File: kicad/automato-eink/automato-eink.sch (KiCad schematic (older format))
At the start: 20 parts

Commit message: finish schematic capture
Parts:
- added J?: Conn_01x08_Male, Connector_PinHeader_2.54mm:PinHeader_1x08_P2.54mm_Vertical, symbol Connector:Conn_01x08_Male
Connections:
- net labels added: BS, BUSY, CS, DC, GDR, HLT_CTL, PREVGH, PREVGL, RESE, RST, SCLK, SDI, TSCL, TSDA
- wire segments 52 -> 74
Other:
- moved on the sheet: C?, D?, J?, L?, Q?, R?

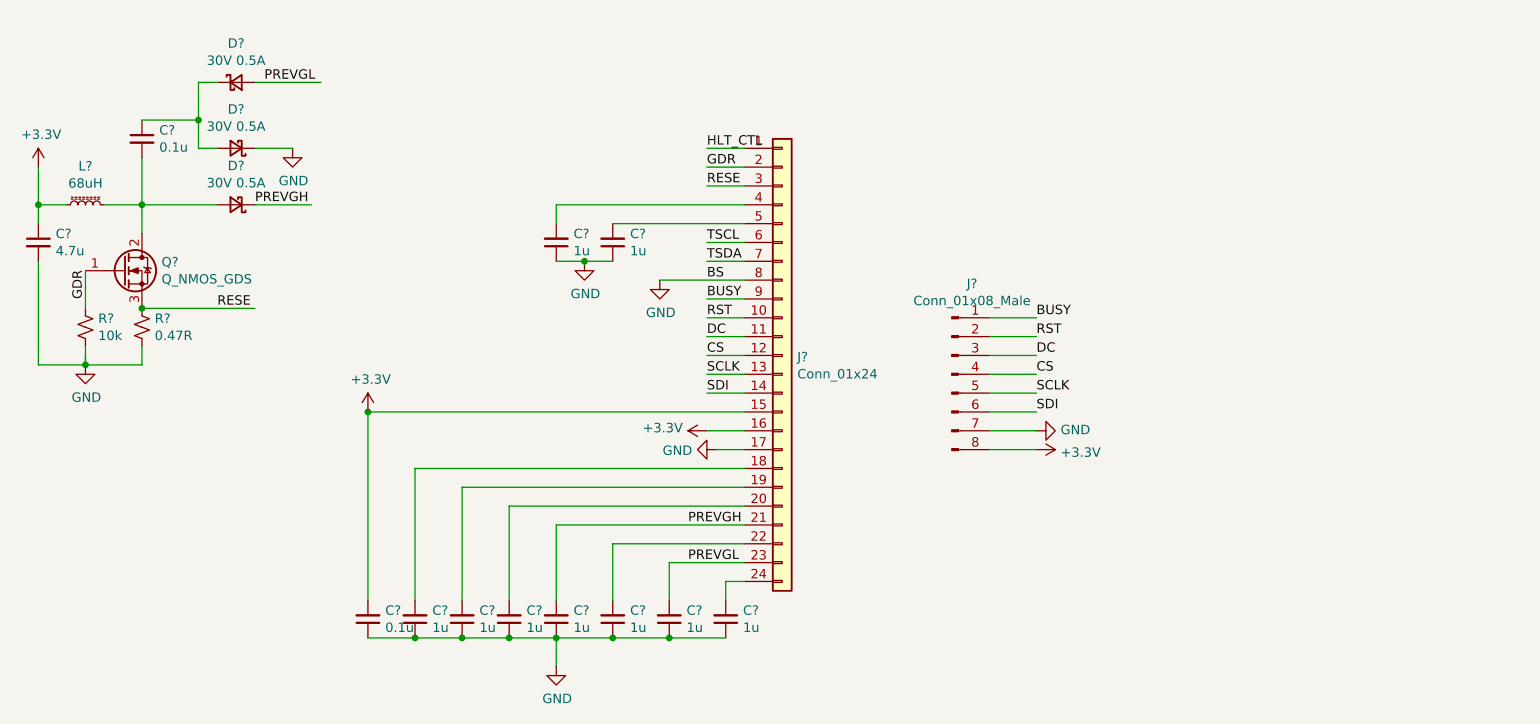
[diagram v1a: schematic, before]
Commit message: added footprints
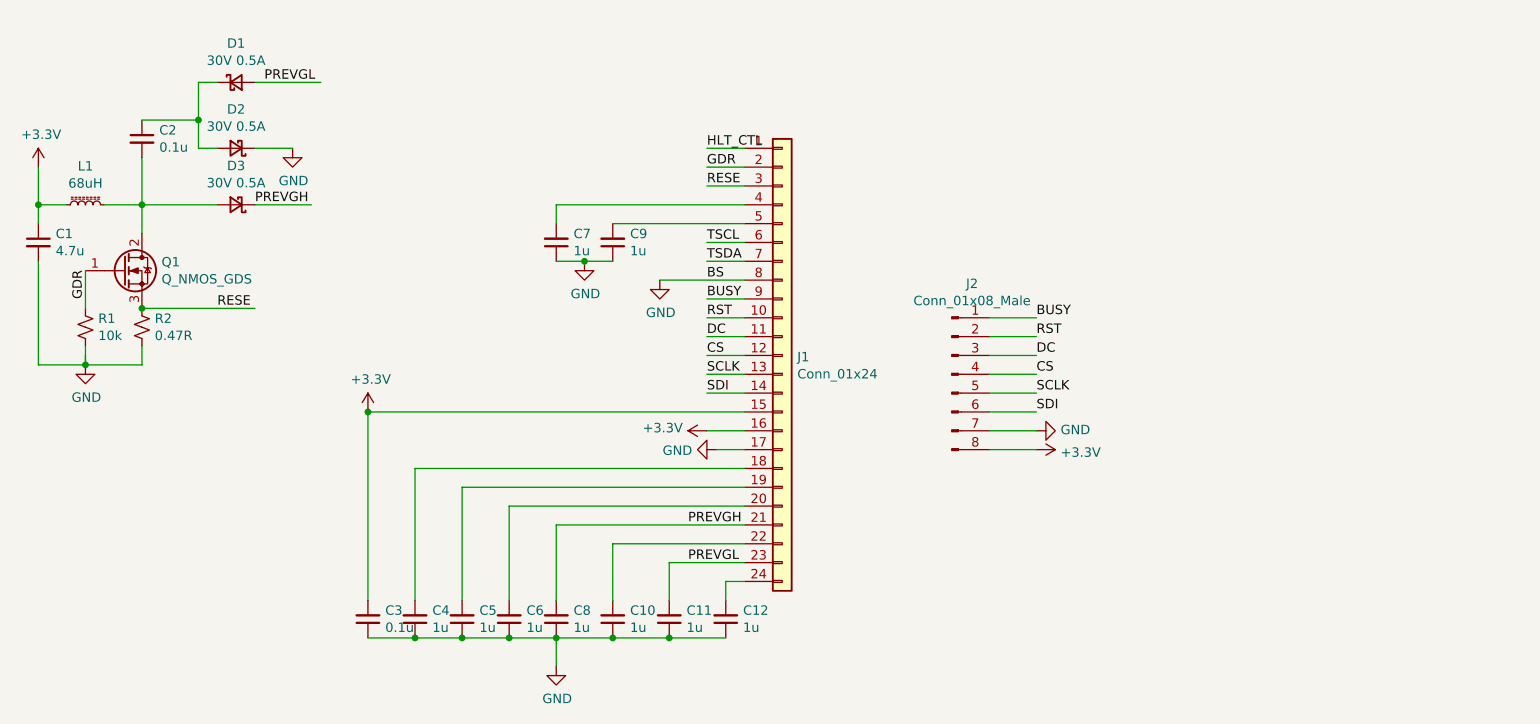
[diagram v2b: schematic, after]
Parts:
- Q1: renamed from Q?; footprint (none) -> Package_TO_SOT_SMD:SOT-23
- gave numbers to parts that had none: 20
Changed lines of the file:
@@
 $EndDescr
 $Comp
-L Connector_Generic:Conn_01x24 J?
+L Connector_Generic:Conn_01x24 J1
 U 1 1 631935D3
 P 6350 3750
-F 0 "J?" H 6430 3742 50  0000 L CNN
+F 0 "J1" H 6430 3742 50  0000 L CNN
 F 1 "Conn_01x24" H 6430 3651 50  0000 L CNN
 F 2 "Connector_FFC-FPC:Hirose_FH12-24S-0.5SH_1x24-1MP_P0.50mm_Horizontal" H 6350 3750 50  0001 C CNN
@@
 $EndComp
 $Comp
-L Device:C_Small C?
+L Device:C_Small C3
 U 1 1 63197FFF
 P 4150 5150
-F 0 "C?" H 4058 5104 50  0000 R CNN
+F 0 "C3" H 4058 5104 50  0000 R CNN
 F 1 "0.1u" H 4058 5195 50  0000 R CNN
 F 2 "Capacitor_SMD:C_0805_2012Metric" H 4150 5150 50  0001 C CNN
@@
 $EndComp
 $Comp
-L Device:C_Small C?
+L Device:C_Small C4
 U 1 1 63197BE1
 P 4400 5150
-F 0 "C?" H 4308 5104 50  0000 R CNN
+F 0 "C4" H 4308 5104 50  0000 R CNN
 F 1 "1u" H 4308 5195 50  0000 R CNN
 F 2 "Capacitor_SMD:C_0805_2012Metric" H 4400 5150 50  0001 C CNN
@@
 $EndComp
 $Comp
-L Device:C_Small C?
+L Device:C_Small C5
 U 1 1 63197900
 P 4650 5150
-F 0 "C?" H 4558 5104 50  0000 R CNN
+F 0 "C5" H 4558 5104 50  0000 R CNN
 F 1 "1u" H 4558 5195 50  0000 R CNN
 F 2 "Capacitor_SMD:C_0805_2012Metric" H 4650 5150 50  0001 C CNN
@@
 $EndComp
 $Comp
-L Device:C_Small C?
+L Device:C_Small C6
 U 1 1 631972BE
 P 4900 5150
-F 0 "C?" H 4808 5104 50  0000 R CNN
+F 0 "C6" H 4808 5104 50  0000 R CNN
 F 1 "1u" H 4808 5195 50  0000 R CNN
 F 2 "Capacitor_SMD:C_0805_2012Metric" H 4900 5150 50  0001 C CNN
@@
 $EndComp
 $Comp
-L Device:C_Small C?
+L Device:C_Small C8
 U 1 1 63196EDB
 P 5150 5150
-F 0 "C?" H 5058 5104 50  0000 R CNN
+F 0 "C8" H 5058 5104 50  0000 R CNN
 F 1 "1u" H 5058 5195 50  0000 R CNN
 F 2 "Capacitor_SMD:C_0805_2012Metric" H 5150 5150 50  0001 C CNN
@@
 $EndComp
 $Comp
-L Device:C_Small C?
+L Device:C_Small C10
 U 1 1 631969B3
 P 5450 5150
-F 0 "C?" H 5358 5104 50  0000 R CNN
+F 0 "C10" H 5358 5104 50  0000 R CNN
 F 1 "1u" H 5358 5195 50  0000 R CNN
 F 2 "Capacitor_SMD:C_0805_2012Metric" H 5450 5150 50  0001 C CNN
@@
 $EndComp
 $Comp
-L Device:C_Small C?
+L Device:C_Small C11
 U 1 1 631962C1
 P 5750 5150
-F 0 "C?" H 5658 5104 50  0000 R CNN
+F 0 "C11" H 5658 5104 50  0000 R CNN
 F 1 "1u" H 5658 5195 50  0000 R CNN
 F 2 "Capacitor_SMD:C_0805_2012Metric" H 5750 5150 50  0001 C CNN
@@
 $EndComp
 $Comp
-L Device:C_Small C?
+L Device:C_Small C12
 U 1 1 63194925
 P 6050 5150
-F 0 "C?" H 5958 5104 50  0000 R CNN
+F 0 "C12" H 5958 5104 50  0000 R CNN
 F 1 "1u" H 5958 5195 50  0000 R CNN
 F 2 "Capacitor_SMD:C_0805_2012Metric" H 6050 5150 50  0001 C CNN
@@
 	5150 5400 5150 5250
 $Comp
-L power:GND #PWR?
+L power:GND #PWR0101
 U 1 1 631A8EC0
 P 5150 5400
-F 0 "#PWR?" H 5150 5150 50  0001 C CNN
+F 0 "#PWR0101" H 5150 5150 50  0001 C CNN
 F 1 "GND" H 5155 5227 50  0000 C CNN
 F 2 "" H 5150 5400 50  0001 C CNN
@@
 $EndComp
 $Comp
-L power:GND #PWR?
+L power:GND #PWR0102
 U 1 1 631A93FC
 P 6000 4250
-F 0 "#PWR?" H 6000 4000 50  0001 C CNN
+F 0 "#PWR0102" H 6000 4000 50  0001 C CNN
 F 1 "GND" V 6005 4122 50  0000 R CNN
 F 2 "" H 6000 4250 50  0001 C CNN
@@
 	6000 4250 6150 4250
 $Comp
-L power:+3.3V #PWR?
+L power:+3.3V #PWR0103
 U 1 1 631AA601
 P 5950 4150
-F 0 "#PWR?" H 5950 4000 50  0001 C CNN
+F 0 "#PWR0103" H 5950 4000 50  0001 C CNN
 F 1 "+3.3V" V 5965 4278 50  0000 L CNN
 F 2 "" H 5950 4150 50  0001 C CNN
@@
 	4150 5050 4150 4050
 $Comp
-L power:+3.3V #PWR?
+L power:+3.3V #PWR0104
 U 1 1 631AB4E3
 P 4150 4050
-F 0 "#PWR?" H 4150 3900 50  0001 C CNN
+F 0 "#PWR0104" H 4150 3900 50  0001 C CNN
 F 1 "+3.3V" H 4165 4223 50  0000 C CNN
 F 2 "" H 4150 4050 50  0001 C CNN
@@
 $EndComp
 $Comp
-L Device:C_Small C?
+L Device:C_Small C7
 U 1 1 631ACF91
 P 5150 3150
-F 0 "C?" H 5058 3104 50  0000 R CNN
+F 0 "C7" H 5058 3104 50  0000 R CNN
 F 1 "1u" H 5058 3195 50  0000 R CNN
 F 2 "Capacitor_SMD:C_0805_2012Metric" H 5150 3150 50  0001 C CNN
@@
 $EndComp
 $Comp
-L Device:C_Small C?
+L Device:C_Small C9
 U 1 1 631AE633
 P 5450 3150
-F 0 "C?" H 5358 3104 50  0000 R CNN
+F 0 "C9" H 5358 3104 50  0000 R CNN
 F 1 "1u" H 5358 3195 50  0000 R CNN
 F 2 "Capacitor_SMD:C_0805_2012Metric" H 5450 3150 50  0001 C CNN
@@
 	5150 3250 5300 3250
 $Comp
-L power:GND #PWR?
+L power:GND #PWR0105
 U 1 1 631B0C8D
 P 5300 3250
-F 0 "#PWR?" H 5300 3000 50  0001 C CNN
+F 0 "#PWR0105" H 5300 3000 50  0001 C CNN
 F 1 "GND" H 5305 3077 50  0000 C CNN
 F 2 "" H 5300 3250 50  0001 C CNN
@@
 	5300 3250 5450 3250
 $Comp
-L Device:D_Schottky_Small D?
+L Device:D_Schottky_Small D2
 U 1 1 631B27DC
 P 3450 2650
-F 0 "D?" H 3450 2443 50  0000 C CNN
+F 0 "D2" H 3450 2443 50  0000 C CNN
 F 1 "30V 0.5A" H 3450 2534 50  0000 C CNN
 F 2 "Diode_SMD:D_SOD-123F" V 3450 2650 50  0001 C CNN
@@
 $EndComp
 $Comp
-L Device:D_Schottky_Small D?
+L Device:D_Schottky_Small D1
 U 1 1 631B34F7
 P 3450 2300
-F 0 "D?" H 3450 2507 50  0000 C CNN
+F 0 "D1" H 3450 2507 50  0000 C CNN
 F 1 "30V 0.5A" H 3450 2416 50  0000 C CNN
 F 2 "Diode_SMD:D_SOD-123F" V 3450 2300 50  0001 C CNN
@@
 $EndComp
 $Comp
-L Device:D_Schottky_Small D?
+L Device:D_Schottky_Small D3
 U 1 1 631B3A21
 P 3450 2950
-F 0 "D?" H 3450 2743 50  0000 C CNN
+F 0 "D3" H 3450 2743 50  0000 C CNN
 F 1 "30V 0.5A" H 3450 2834 50  0000 C CNN
 F 2 "Diode_SMD:D_SOD-123F" V 3450 2950 50  0001 C CNN
@@
 $EndComp
 $Comp
-L Device:C_Small C?
+L Device:C_Small C2
 U 1 1 631B4810
 P 2950 2600
-F 0 "C?" H 3042 2646 50  0000 L CNN
+F 0 "C2" H 3042 2646 50  0000 L CNN
 F 1 "0.1u" H 3042 2555 50  0000 L CNN
 F 2 "Capacitor_SMD:C_0805_2012Metric" H 2950 2600 50  0001 C CNN
@@
 	2950 2950 3350 2950
 $Comp
-L Device:L_Core_Ferrite_Small L?
+L Device:L_Core_Ferrite_Small L1
 U 1 1 631B7739
 P 2650 2950
-F 0 "L?" V 2855 2950 50  0000 C CNN
+F 0 "L1" V 2855 2950 50  0000 C CNN
 F 1 "68uH" V 2764 2950 50  0000 C CNN
 F 2 "" H 2650 2950 50  0001 C CNN
@@
 Connection ~ 2950 2950
 $Comp
-L Device:C_Small C?
+L Device:C_Small C1
 U 1 1 631BA6FA
 P 2400 3150
-F 0 "C?" H 2492 3196 50  0000 L CNN
+F 0 "C1" H 2492 3196 50  0000 L CNN
 F 1 "4.7u" H 2492 3105 50  0000 L CNN
 F 2 "Capacitor_SMD:C_0805_2012Metric" H 2400 3150 50  0001 C CNN
@@
 Connection ~ 2400 2950
 $Comp
-L power:+3.3V #PWR?
+L power:+3.3V #PWR0106
 U 1 1 631BE889
 P 2400 2750
-F 0 "#PWR?" H 2400 2600 50  0001 C CNN
+F 0 "#PWR0106" H 2400 2600 50  0001 C CNN
 F 1 "+3.3V" H 2415 2923 50  0000 C CNN
 F 2 "" H 2400 2750 50  0001 C CNN
@@
 	3550 2650 3750 2650
 $Comp
-L power:GND #PWR?
+L power:GND #PWR0107
 U 1 1 631C2486
 P 3750 2650
-F 0 "#PWR?" H 3750 2400 50  0001 C CNN
+F 0 "#PWR0107" H 3750 2400 50  0001 C CNN
 F 1 "GND" H 3755 2477 50  0000 C CNN
 F 2 "" H 3750 2650 50  0001 C CNN
@@
 $EndComp
 $Comp
-L Device:Q_NMOS_GDS Q?
+L Device:Q_NMOS_GDS Q1
 U 1 1 631C3192
 P 2850 3300
-F 0 "Q?" H 3054 3346 50  0000 L CNN
+F 0 "Q1" H 3054 3346 50  0000 L CNN
 F 1 "Q_NMOS_GDS" H 3054 3255 50  0000 L CNN
-F 2 "" H 3050 3400 50  0001 C CNN
+F 2 "Package_TO_SOT_SMD:SOT-23" H 3050 3400 50  0001 C CNN
 F 3 "~" H 2850 3300 50  0001 C CNN
 	1    2850 3300
@@
 	2950 2950 2950 3100
 $Comp
-L Device:R_Small_US R?
+L Device:R_Small_US R1
 U 1 1 631C5AB5
 P 2650 3600
-F 0 "R?" H 2718 3646 50  0000 L CNN
+F 0 "R1" H 2718 3646 50  0000 L CNN
 F 1 "10k" H 2718 3555 50  0000 L CNN
 F 2 "Resistor_SMD:R_0805_2012Metric" H 2650 3600 50  0001 C CNN
@@
 	2650 3300 2650 3500
 $Comp
-L power:GND #PWR?
+L power:GND #PWR0108
 U 1 1 631C71F5
 P 2650 3800
-F 0 "#PWR?" H 2650 3550 50  0001 C CNN
+F 0 "#PWR0108" H 2650 3550 50  0001 C CNN
 F 1 "GND" H 2655 3627 50  0000 C CNN
 F 2 "" H 2650 3800 50  0001 C CNN
@@
 Connection ~ 2650 3800
 $Comp
-L Device:R_Small_US R?
+L Device:R_Small_US R2
 U 1 1 631CAA59
 P 2950 3600
-F 0 "R?" H 3018 3646 50  0000 L CNN
+F 0 "R2" H 3018 3646 50  0000 L CNN
 F 1 "0.47R" H 3018 3555 50  0000 L CNN
 F 2 "Resistor_SMD:R_0805_2012Metric" H 2950 3600 50  0001 C CNN
@@
 GDR
 $Comp
-L power:GND #PWR?
+L power:GND #PWR0109
 U 1 1 631E825C
 P 5700 3350
-F 0 "#PWR?" H 5700 3100 50  0001 C CNN
+F 0 "#PWR0109" H 5700 3100 50  0001 C CNN
 F 1 "GND" H 5705 3177 50  0000 C CNN
 F 2 "" H 5700 3350 50  0001 C CNN
@@
 	5700 3350 6150 3350
 $Comp
-L Connector:Conn_01x08_Male J?
+L Connector:Conn_01x08_Male J2
 U 1 1 631F46FA
 P 7250 3850
-F 0 "J?" H 7358 4331 50  0000 C CNN
+F 0 "J2" H 7358 4331 50  0000 C CNN
 F 1 "Conn_01x08_Male" H 7358 4240 50  0000 C CNN
 F 2 "Connector_PinHeader_2.54mm:PinHeader_1x08_P2.54mm_Vertical" H 7250 3850 50  0001 C CNN
@@
 SDI
 $Comp
-L power:GND #PWR?
+L power:GND #PWR0110
 U 1 1 63204BD1
 P 7700 4150
-F 0 "#PWR?" H 7700 3900 50  0001 C CNN
+F 0 "#PWR0110" H 7700 3900 50  0001 C CNN
 F 1 "GND" V 7705 4022 50  0000 R CNN
 F 2 "" H 7700 4150 50  0001 C CNN
@@
 $EndComp
 $Comp
-L power:+3.3V #PWR?
+L power:+3.3V #PWR0111
 U 1 1 63205191
 P 7700 4250
-F 0 "#PWR?" H 7700 4100 50  0001 C CNN
+F 0 "#PWR0111" H 7700 4100 50  0001 C CNN
 F 1 "+3.3V" V 7715 4378 50  0000 L CNN
 F 2 "" H 7700 4250 50  0001 C CNN

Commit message: add inductor footprint
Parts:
- L1: footprint (none) -> Inductor_SMD:L_7.3x7.3_H3.5
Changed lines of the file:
@@
 F 0 "L1" V 2855 2950 50  0000 C CNN
 F 1 "68uH" V 2764 2950 50  0000 C CNN
-F 2 "" H 2650 2950 50  0001 C CNN
+F 2 "Inductor_SMD:L_7.3x7.3_H3.5" H 2650 2950 50  0001 C CNN
 F 3 "~" H 2650 2950 50  0001 C CNN
 	1    2650 2950
